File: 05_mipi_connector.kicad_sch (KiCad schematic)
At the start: 0 parts

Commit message: added mipi connector
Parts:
- added C?: 0.1u, Capacitor_SMD:C_0603_1608Metric, symbol Device:C
- added J?: Conn_01x22, Connector_FFC-FPC:Hirose_FH12-22S-0.5SH_1x22-1MP_P0.50mm_Horizontal, symbol Connector_Generic:Conn_01x22
- added R?: 0, Resistor_SMD:R_0603_1608Metric, symbol Device:R
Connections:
- new net +3.3V: R?.2
- new net CAM_IO0: J?.6 (Pin_6)
- new net CAM_IO1: J?.5 (Pin_5)
- new net GND: C?.2, J?.10 (Pin_10), J?.13 (Pin_13), J?.16 (Pin_16), J?.19 (Pin_19), J?.22 (Pin_22), J?.4 (Pin_4), J?.7 (Pin_7)
- new net MIPI_CLK_N: J?.15 (Pin_15)
- new net MIPI_CLK_P: J?.14 (Pin_14)
- new net MIPI_D0_N: J?.21 (Pin_21)
- new net MIPI_D0_P: J?.20 (Pin_20)
- new net MIPI_D1_N: J?.18 (Pin_18)
- new net MIPI_D1_P: J?.17 (Pin_17)
- new net MIPI_D2_N: J?.12 (Pin_12)
- new net MIPI_D2_P: J?.11 (Pin_11)
- new net MIPI_D3_N: J?.9 (Pin_9)
- new net MIPI_D3_P: J?.8 (Pin_8)
- new net MIPI_I2C_SCL: J?.3 (Pin_3)
- new net MIPI_I2C_SDA: J?.2 (Pin_2)
- new net VCC_CAM: C?.1, J?.1 (Pin_1), R?.1

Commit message: finished first pass of the schematics
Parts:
- removed J?: Conn_01x22, Connector_FFC-FPC:Hirose_FH12-22S-0.5SH_1x22-1MP_P0.50mm_Horizontal, symbol Connector_Generic:Conn_01x22
- added J?: Conn_01x22, Connector_FFC-FPC:Hirose_FH12-22S-0.5SH_1x22-1MP_P0.50mm_Horizontal, symbol Connector_Generic:Conn_01x22
- added R? (x2): 10k, Resistor_SMD:R_0603_1608Metric, symbol Device:R
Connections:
- net CAM_IO0: now also J?.17 (Pin_17)
- net CAM_IO1: now also J?.18 (Pin_18)
- net GND: now also J?.1 (Pin_1), J?.10 (Pin_10), J?.13 (Pin_13), J?.16 (Pin_16), J?.19 (Pin_19), J?.4 (Pin_4), J?.7 (Pin_7)
- net MIPI_CLK_N: now also J?.8 (Pin_8)
- net MIPI_CLK_P: now also J?.9 (Pin_9)
- net MIPI_D0_N: now also J?.2 (Pin_2)
- net MIPI_D0_P: now also J?.3 (Pin_3)
- net MIPI_D1_N: now also J?.5 (Pin_5)
- net MIPI_D1_P: now also J?.6 (Pin_6)
- net MIPI_D2_N: now also J?.11 (Pin_11)
- net MIPI_D2_P: now also J?.12 (Pin_12)
- net MIPI_D3_N: now also J?.14 (Pin_14)
- net MIPI_D3_P: now also J?.15 (Pin_15)
- net MIPI_I2C_SCL: now also J?.20 (Pin_20), R?.2
- net MIPI_I2C_SDA: now also J?.21 (Pin_21), R?.2
- net VCC_CAM: now also J?.22 (Pin_22)
- new net +3V3: R?.1, R?.1

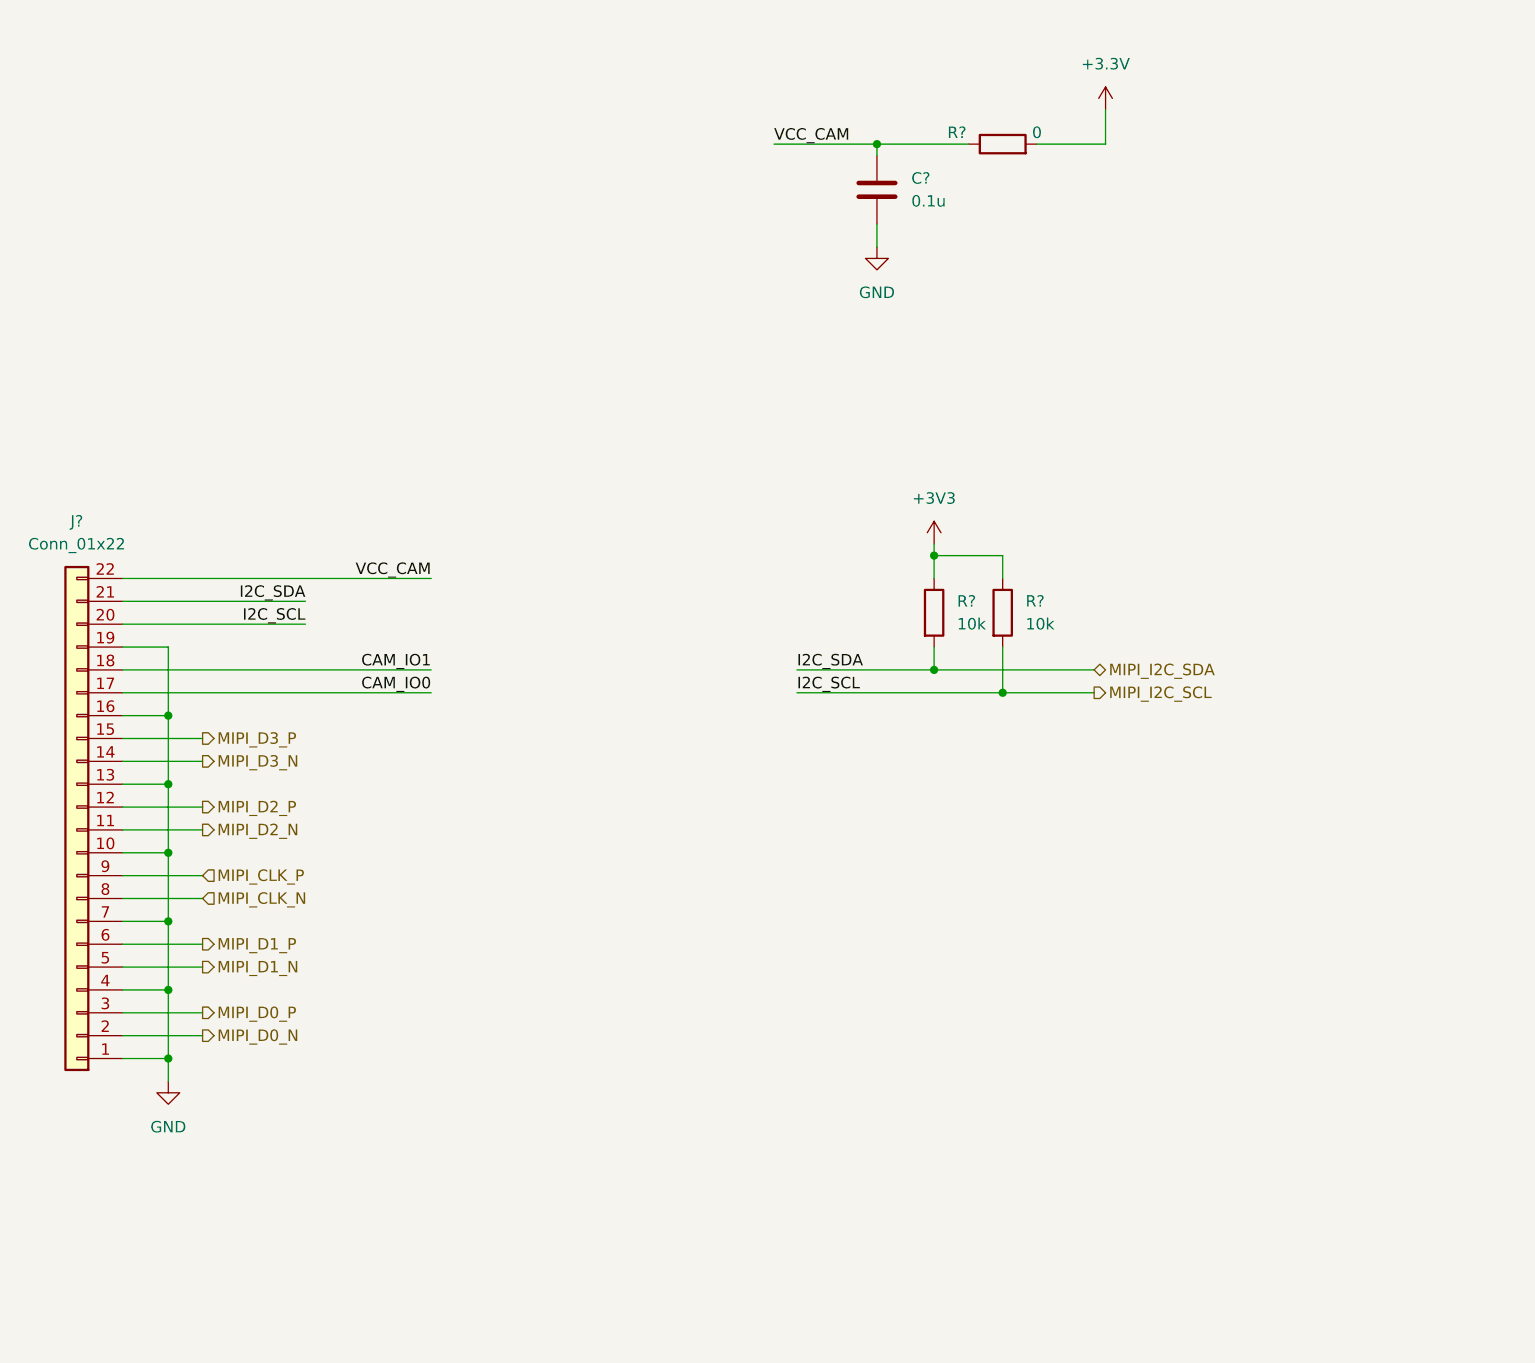
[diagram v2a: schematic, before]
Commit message: cleaned up some DRC errors
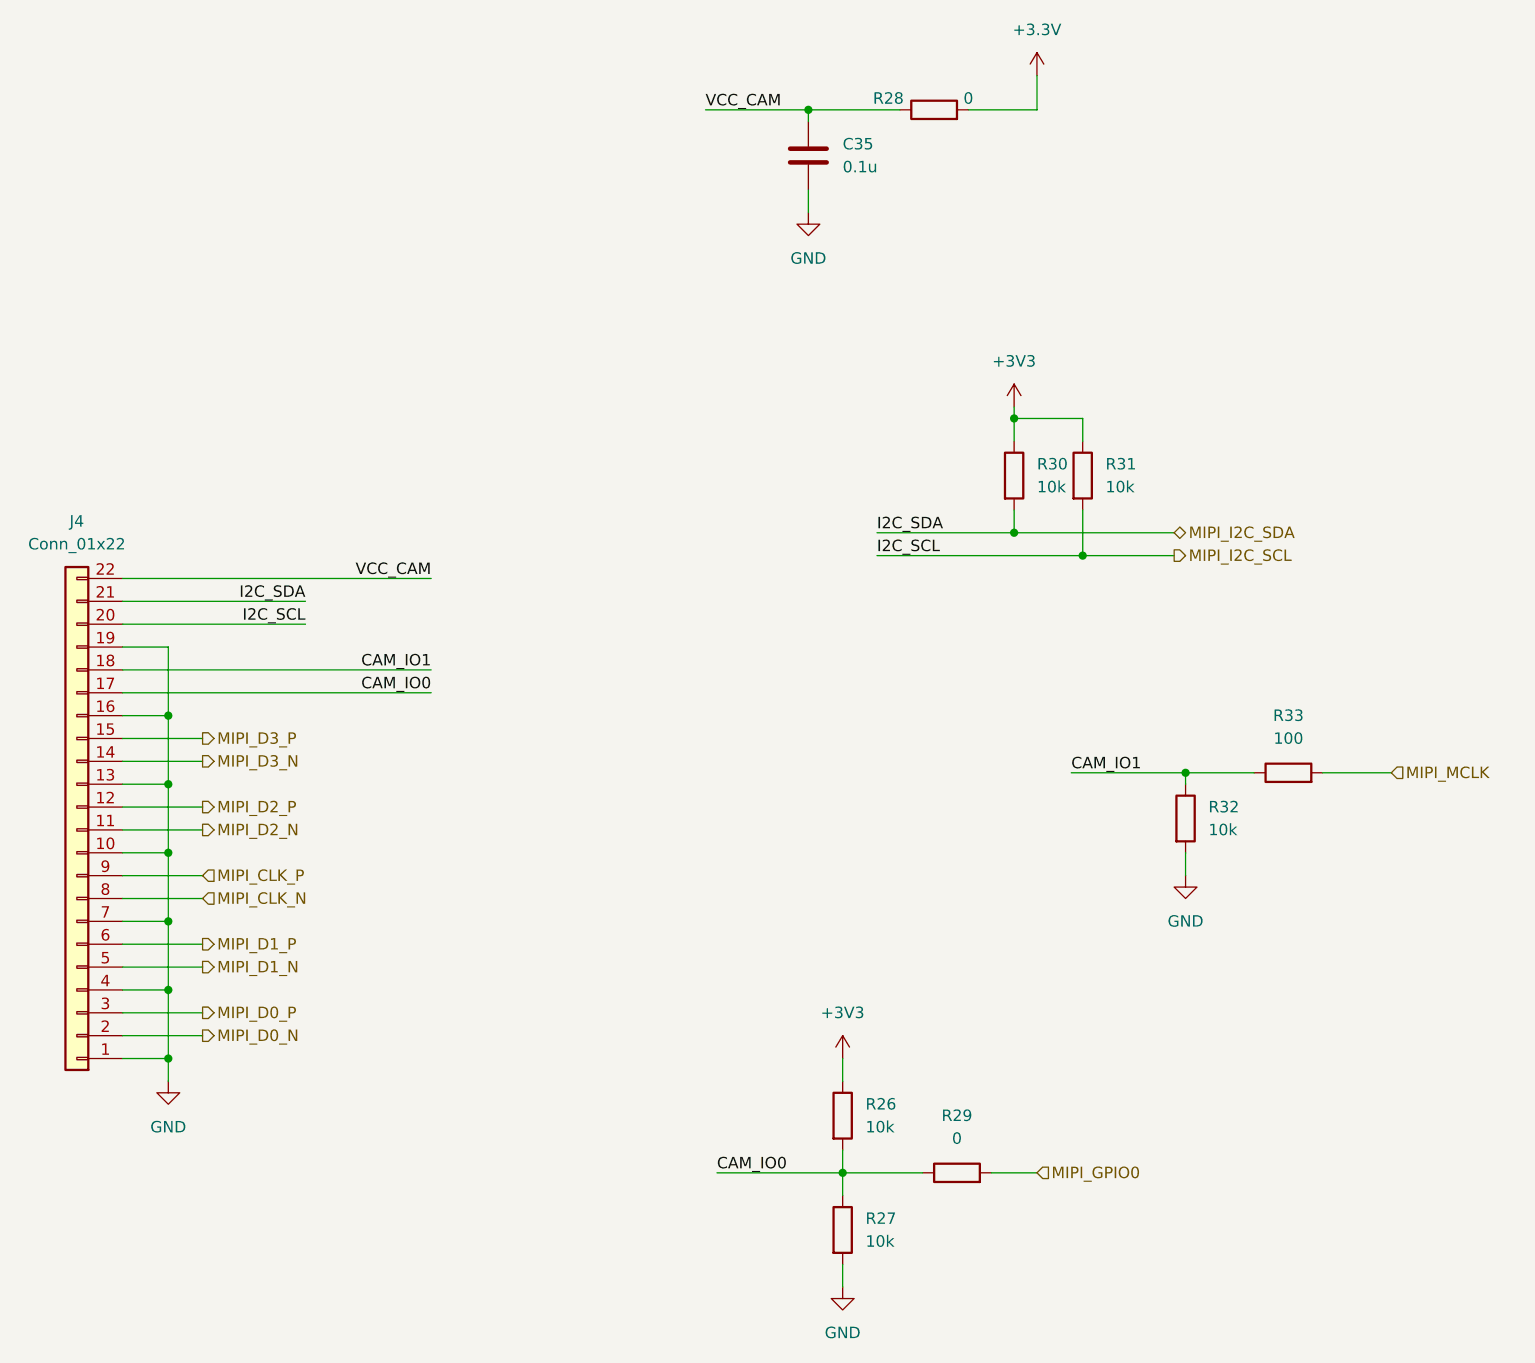
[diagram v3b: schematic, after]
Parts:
- added R26, R27, R32: 10k, Resistor_SMD:R_0603_1608Metric, symbol Device:R
- added R29: 0, Resistor_SMD:R_0603_1608Metric, symbol Device:R
- added R33: 100, Resistor_SMD:R_0603_1608Metric, symbol Device:R
- gave numbers to parts that had none: 5
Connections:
- net +3V3: now also R26.1
- net CAM_IO0: now also R26.2, R27.1, R29.1
- net CAM_IO1: now also R32.1, R33.1
- net GND: now also R27.2, R32.2
- new net MIPI_GPIO0: R29.2
- new net MIPI_MCLK: R33.2
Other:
- moved on the sheet: C35, R28, R30, R31

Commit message: finished schematics
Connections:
- net +3.3V is gone; now on net +3V3: R28.2
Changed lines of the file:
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@@
     (effects (font (size 1.27 1.27)) (justify left))
+  )
+  (symbol (lib_id "power:+3V3") (at 143.51 29.21 0) (unit 1)
+    (in_bom yes) (on_board yes)
+    (property "Reference" "#PWR0122" (id 0) (at 143.51 33.02 0)
+      (effects (font (size 1.27 1.27)) hide)
+    )
+    (property "Value" "+3V3" (id 1) (at 143.891 24.8158 0))
+    (property "Footprint" "" (id 2) (at 143.51 29.21 0)
+      (effects (font (size 1.27 1.27)) hide)
+    )
+    (property "Datasheet" "" (id 3) (at 143.51 29.21 0)
+      (effects (font (size 1.27 1.27)) hide)
+    )
+    (pin "1")
   )
   (symbol (lib_id "Device:C") (at 118.11 38.1 0) (unit 1)
@@
     (pin "2")
   )
-  (symbol (lib_id "power:+3.3V") (at 143.51 29.21 0) (unit 1)
-    (in_bom yes) (on_board yes) (fields_autoplaced)
-    (property "Reference" "#PWR096" (id 0) (at 143.51 33.02 0)
-      (effects (font (size 1.27 1.27)) hide)
-    )
-    (property "Value" "+3.3V" (id 1) (at 143.51 24.13 0))
-    (property "Footprint" "" (id 2) (at 143.51 29.21 0)
-      (effects (font (size 1.27 1.27)) hide)
-    )
-    (property "Datasheet" "" (id 3) (at 143.51 29.21 0)
-      (effects (font (size 1.27 1.27)) hide)
-    )
-    (pin "1")
-  )
   (symbol (lib_id "Device:R") (at 121.92 144.78 0) (unit 1)
